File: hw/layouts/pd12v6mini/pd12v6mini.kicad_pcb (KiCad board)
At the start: 4 copper layers, 33 x 20 mm, 28 parts

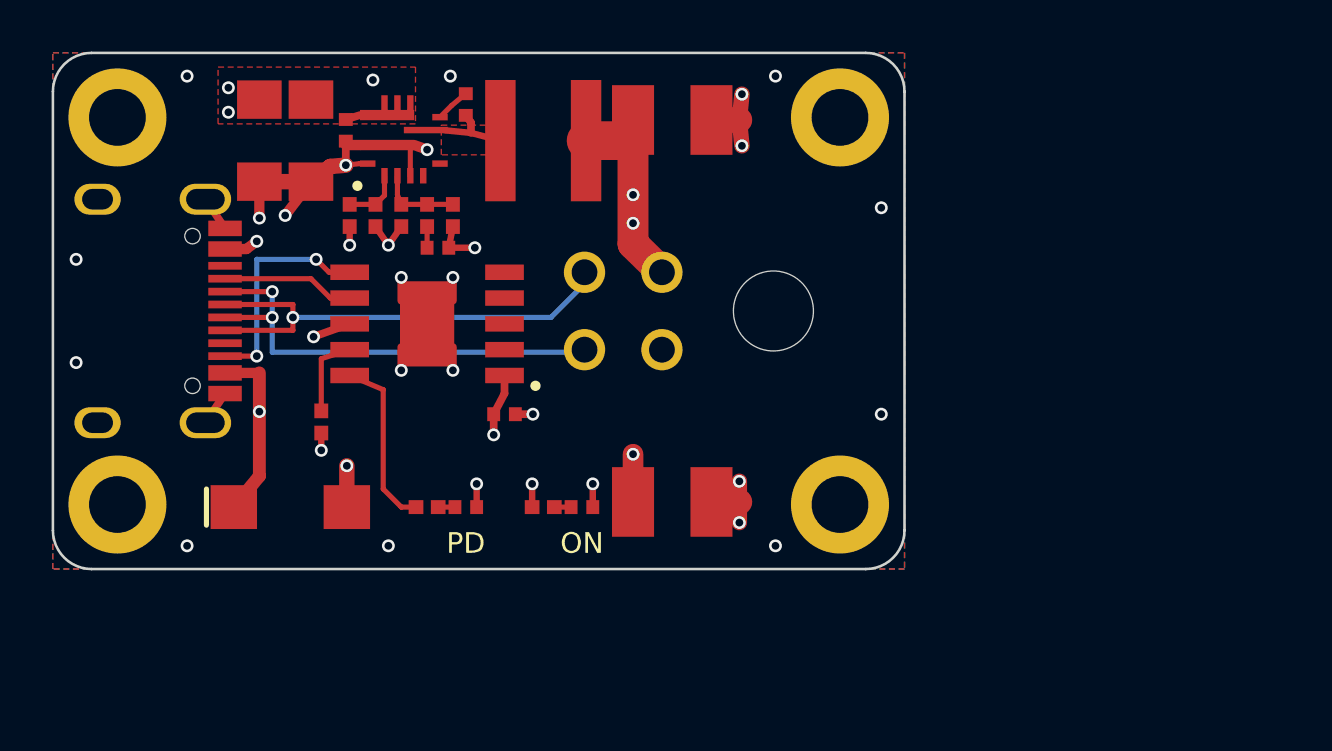
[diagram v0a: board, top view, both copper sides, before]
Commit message: pd12v6mini rev B: grouped hand layout, every part labelled, consistent routing
- 35x24.5 mm: INPUT left, BUCK along the top with a 2 mm-pitch control row,
  PD controller centred with mirrored PD/ON status columns, output caps
  mirrored about the Micro-Fit. White inset outline restored, holes inset.
- Routing redone: one width per job (0.2 sig / 0.3 tap / 0.6 power), straight
  pad exits, uniform 45-degree chamfers, top layer pad-to-pad only (USB data
  on B.Cu, CC2 on In2, power via In2 pours). DRC clean, 0 unconnected.

Co-Authored-By: Claude Opus 5.5 <noreply@anthropic.com>
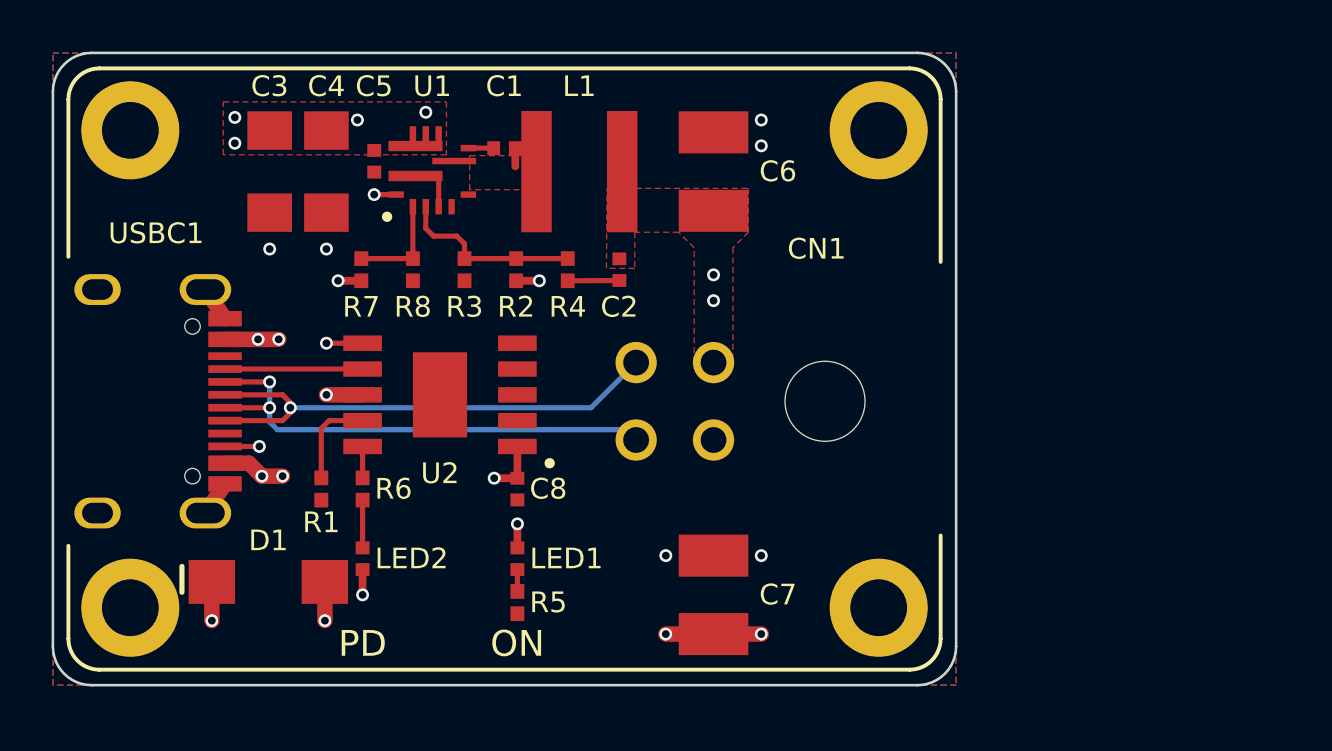
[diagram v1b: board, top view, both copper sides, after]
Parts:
- moved C2 7.08 mm to (21.9, 8.40), turned to -90 degrees
- moved R4 5.84 mm to (19.9, 8.40)
- moved LED2 4.47 mm to (12.0, 19.6), turned to -90 degrees
- moved H4 4.27 mm to (32.0, 21.5)
- moved CN1 4.03 mm to (24.1, 13.5)
- moved H3 4.03 mm to (3.00, 21.5)
- moved C7 3.94 mm to (25.6, 21.0), turned to 90 degrees
- moved R5 3.83 mm to (18.0, 21.3), turned to -90 degrees
- moved USBC1 3.50 mm to (4.20, 13.5)
- moved R2 3.23 mm to (17.9, 8.40)
- moved R3 3.23 mm to (15.9, 8.40)
- moved LED1 3.20 mm to (18.0, 19.6), turned to 90 degrees
- moved D1 3.02 mm to (8.35, 20.5)
- moved C8 2.94 mm to (18.0, 16.9), turned to -90 degrees
- moved U2 2.80 mm to (15.0, 13.2)
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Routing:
- net GND: track 28.2 -> 6.06 mm, vias 27 -> 8
- net VOUT: track 12.0 -> 5.53 mm, vias 5 -> 6
- net PG_n: track 6.82 -> 1.22 mm
- net FB: track 3.14 -> 7.16 mm
- net VBUS: track 14.3 -> 11.4 mm, vias 9 -> 13
- net SW: track 2.93 -> 0.71 mm
- net EN: track 2.25 -> 4.01 mm
- net USB_DN: track 18.1 -> 19.5 mm
- net USB_DP: track 18.5 -> 19.8 mm
- net LED_PD_K: track 0.65 -> 1.85 mm
- net FF: track 0.82 -> 2.00 mm
- added copper zone on F.Cu, net VOUT
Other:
- board size 33 x 20 mm -> 35 x 24.5 mm
- board text added: "rev B 2026-10"
- board text removed: "rev A 2026-10"

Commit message: pd12v6mini rev E: 6.8 uH 12.5 A inductor, third input cap, 47.5 x 25 mm
TI WEBENCH (real TPS56637 model) flagged the 5.6 uH / 8.6 A Isat inductor (overload peak
~10 A) and ~8 uF effective input capacitance. Rev E uses PROD PSTMAA666460-6R8MB (C55172548)
and adds C9 (10 uF 1206, Basic). Re-sim: settling 0.14 ms, 1.6 W lost at 20 V / 5 A.

- revs B, C, D kept in hw/layouts/pd12v6mini_revX
- CC2 rerouted clear of the back text; VOUT strip clear of the CN1 label
- ngspice buck and UVLO decks in hw/sim
- scripts/fab_export.sh: JLCPCB gerber zip, BOM and CPL from the stored fill
- docs/pd12v6/mini.md: WEBENCH results, JLCPCB quote so far, DIY parts cost

Co-Authored-By: Claude Opus 5.5 <noreply@anthropic.com>
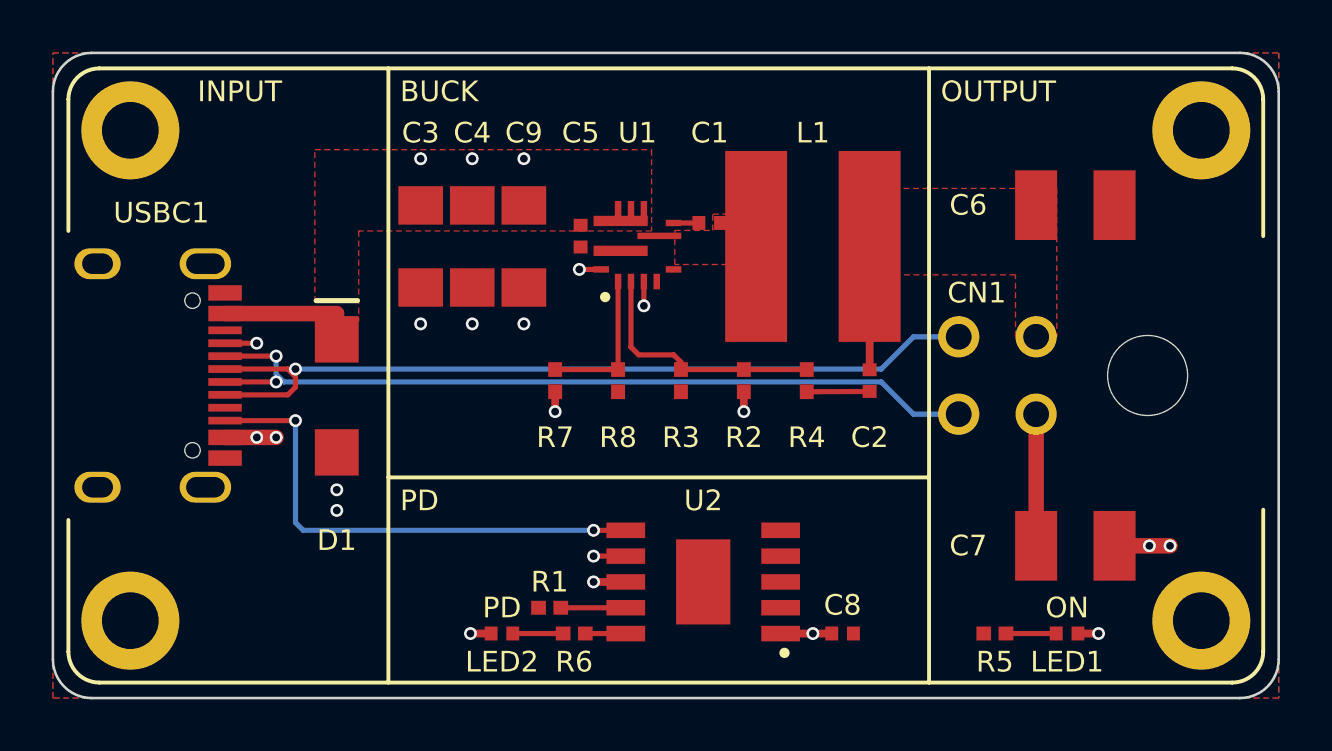
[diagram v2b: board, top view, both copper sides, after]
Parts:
- added C9: , SAMSUNG_CL31A106KBHNNNE:C1206, F.Cu at (18.2, 7.50)
- L1: footprint YJYCOIN_YSPIT0550A_5R6M:IND-SMD_L5.5-W5.3 -> PROD_PSTMAA666460_6R8MB:IND-SMD_PSTMAA666460-6R8MB
- R8: footprint UNI_ROYAL_0402WGF2702TCE:R0402 -> UNI_ROYAL_0402WGF3002TCE:R0402
- moved LED1 21.5 mm to (39.3, 22.5), turned to 0 degrees
- moved R5 18.5 mm to (36.5, 22.5), turned to 180 degrees
- moved C7 14.1 mm to (39.6, 19.1), turned to 180 degrees
- moved C6 14.1 mm to (39.6, 5.90), turned to 0 degrees
- moved C8 13.8 mm to (30.6, 22.5), turned to 0 degrees
- moved CN1 12.5 mm to (36.6, 12.5)
- moved U2 12.5 mm to (25.2, 20.5)
- moved H4 12.5 mm to (44.5, 22.0)
- moved H2 12.5 mm to (44.5, 3.00)
- moved C2 10.6 mm to (31.6, 12.7)
- moved R4 10.2 mm to (29.2, 12.7)
- moved R1 9.97 mm to (19.2, 21.5), turned to 180 degrees
- moved R6 9.93 mm to (20.2, 22.5), turned to 0 degrees
- moved R2 9.82 mm to (26.8, 12.7)
- moved L1 9.50 mm to (29.4, 7.50)
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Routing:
- net CC1: track 5.33 -> 19.8 mm, vias 0 -> 2
- net USB_DP: track 19.8 -> 32.3 mm
- net USB_DN: track 19.5 -> 31.8 mm
- net CC2: track 8.98 -> 19.6 mm
- net FB: track 7.16 -> 9.88 mm
- net EN: track 4.01 -> 5.85 mm
- net CFG1: track 3.64 -> 2.52 mm
- net LED_OUT_K: track 0.85 -> 1.95 mm
- net GND: track 6.06 -> 6.89 mm, vias 8 -> 7
- net VOUT: track 5.53 -> 4.80 mm, vias 6 -> 4
- net SW: track 0.71 -> 0.00 mm
- net VBUS: track 11.4 -> 11.1 mm, vias 13 -> 9
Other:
- board size 35 x 24.5 mm -> 47.5 x 25 mm
- board text added: "BUCK"
- board text added: "INPUT"
- board text added: "OUTPUT"
- board text added: "rev E 2026-10"
- board text removed: "rev B 2026-10"
